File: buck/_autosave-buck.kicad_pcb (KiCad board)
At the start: 2 copper layers, 37.8 x 17.8 mm, 15 parts, among them IC1 TPS630702RNMR

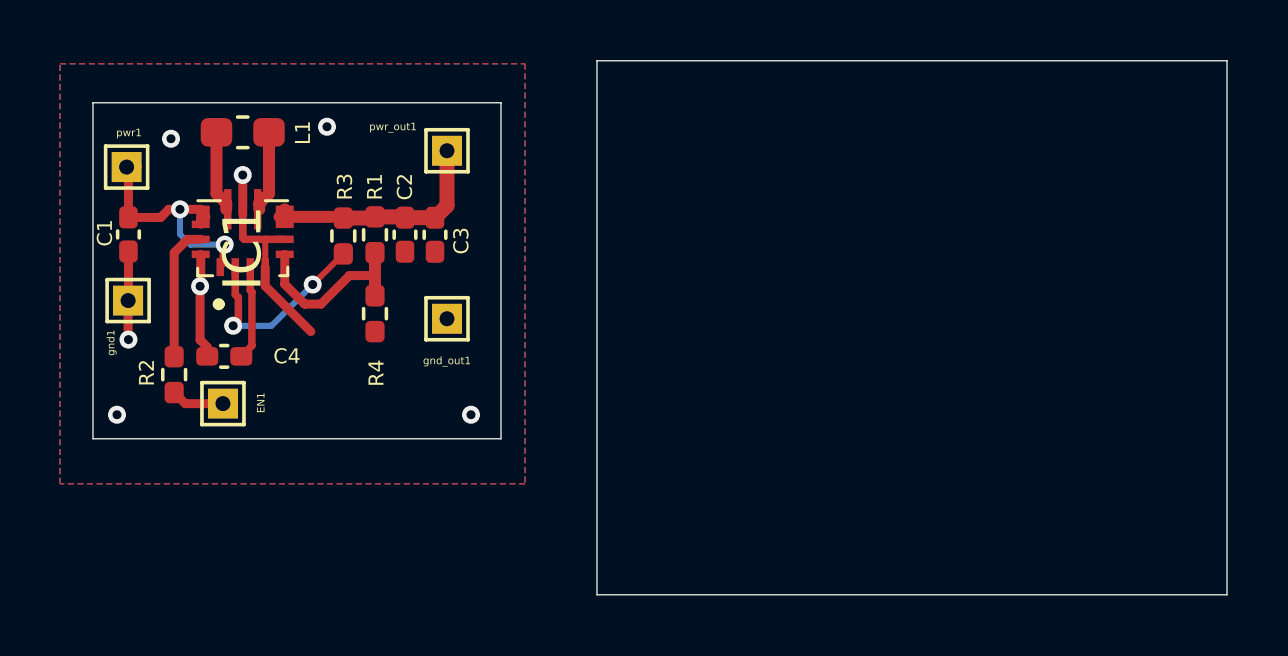
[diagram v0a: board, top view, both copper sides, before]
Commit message: add through hole solder spots as per request
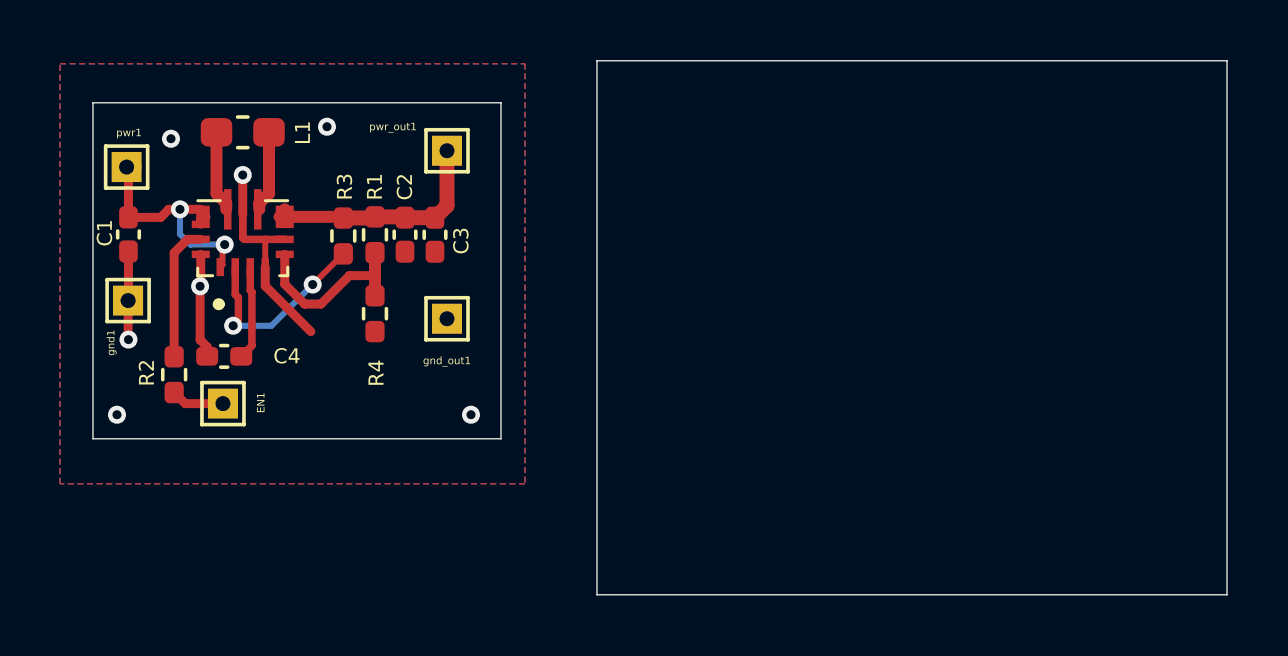
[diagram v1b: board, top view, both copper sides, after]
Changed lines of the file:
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@@
 			(at 0.194 0 90)
 			(layer "F.SilkS")
+			(hide yes)
 			(effects
 				(font
@@
 			(layer "F.Fab")
 		)
-		(fp_text user "${REFERENCE}"
-			(at 0.194 0 90)
-			(layer "F.Fab")
-			(effects
-				(font
-					(size 1.27 1.27)
-					(thickness 0.254)
-				)
-			)
-		)
 		(pad "1" smd rect
